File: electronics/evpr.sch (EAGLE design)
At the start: 93 parts, among them J1 10118193-0001LF, J2 B4P-VH(LF)(SN), Q1 AOD4184A, Q2 AOD4184A, T1 MMBT2222A, T2 MMBT2222A, T3 MMBT2222A, T5 MMBT2222A, U1 MC14044BDR2G, U2 BQ2057TTS, U3 ESP32-WROOM-32D, U5 AP2112K-3.3TRG1, U6 SN74AHCT125DR, U7 TPSM84824MOLR, U8 LTC4353CMSPBFMSOP-16_MS-M, X1 B3P-VH(LF)(SN), X2 B3P-VH(LF)(SN), X3 B3P-VH(LF)(SN)

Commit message: routing and board fixes
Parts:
- added U$13, U$15: LSM115J, mccloud:LSM115J
- C1: value 10sµF -> 10µF
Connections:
- new net AGND: R2.2, R31.2, R32.2, U7.AGND, U7.AGND_2, U7.AGND_3
- new net N$43: R7.2, R8.2, U$13.C, U$15.C, U1.!R1, U1.!R2, U1.!R3, U1.!S1, U1.!S2, U1.!S3, U1.E, U1.VDD
- net GND: no longer R2.2, R31.2, R32.2, U7.AGND, U7.AGND_2, U7.AGND_3
- net VBAT: now also U$15.A
- net VRAW: now also U$13.A; no longer R7.2, R8.2, U1.!R1, U1.!R2, U1.!R3, U1.!S1, U1.!S2, U1.!S3, U1.E, U1.VDD

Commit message: Whew. Lots of routing. Lots of minor circuit changes. Routing is 99% done, just finishing touches are remaining.
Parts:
- removed R11: 10k, rcl:R-US_R0805
- added C11, C21: 0.1uF, eagle-ltspice:CC0603
- U$13: value LSM115J -> SDM40E20LC; device mccloud:LSM115J -> mccloud:SDM40E20LC
- U$15: value LSM115J -> 1000µF; device mccloud:LSM115J -> mccloud:810RADCAP; COMPONENT (none) -> UWT0J102MNL1GS
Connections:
- net 5.0V: now also C21.2
- net GND: now also C11.1, C21.1, U$15.-; no longer R11.1
- net N$28: now also U$15.+
- net N$43: now also C11.2; no longer U$15.C
- net POWERSAVE: no longer R11.2
- net VBAT: now also U$13.A1; no longer U$15.A
- net VRAW: now also U$13.A2; no longer U$13.A
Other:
- moved on the sheet: F1, J2, JP1, U$2, U$7, X2, X3

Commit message: Routing complete. All DRC/ERC checks except for USB port silliness performed and resolved. Test points added.
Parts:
- added TP1, TP10, TP11, TP12, TP13, TP14, TP15, TP16, TP19, TP2, TP20, TP21, TP22, TP23, TP3, TP4, TP5, TP6, TP7, TP8, TP9: PTR1TP10R, testpad:PTR1TP10R
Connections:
- net 3.3V: now also TP12.TP
- net 5.0V: now also TP11.TP, U6.!1OE, U6.!2OE, U6.1A, U6.2A
- net AGND: now also TP7.TP
- net BOOTMODE: now also TP14.TP
- net GND: now also U6.!3OE, U6.!4OE
- net N$11: now also TP22.TP
- net N$14: now also TP10.TP
- net N$18: now also TP15.TP
- net N$19: now also TP16.TP
- net N$30: now also TP21.TP
- net N$35: now also TP8.TP
- net N$43: now also TP23.TP
- net N$51: now also TP9.TP
- net POWERSAVE: now also TP4.TP
- net RESET: now also TP13.TP
- net SHUTDOWN: now also TP19.TP
- net SHUTDOWN_CANCEL: now also TP20.TP
- net TACH_RAW: now also TP2.TP
- net USBD+: no longer J1.ID
- net VBAT: now also TP6.TP
- net VCONV: now also TP5.TP
- net VRAW: now also TP3.TP
- net VRAW_PF: now also TP1.TP
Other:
- moved on the sheet: C9, J1, R21, R23, R30

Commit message: Final  changes before prototype run
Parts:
- removed TP1: PTR1TP10R, testpad:PTR1TP10R
- removed U$6: 8A, mccloud:0437008.WR
- added SJ1: (no value), jumper:SJ
- added U$16: (no value), mccloud:VESD16A2-03G-G3-08
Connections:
- removed net VRAW_PF: TP1.TP, U$6.1, X1.2
- net GND: now also SJ1.1, U$16.AA
- net N$30: now also SJ1.2
- net SYS_POWER: now also Q1.D, Q2.D; no longer Q1.S, Q2.S
- net TACH_RAW: now also U$16.K1
- net VBAT: now also Q2.S; no longer Q2.D
- net VCONV: now also Q1.S; no longer Q1.D
- net VRAW: now also U$16.K2, X1.2; no longer U$6.2
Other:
- moved on the sheet: C6, C7, C8, LED1, Q1, Q2, R15, R20, R21, R22, R23, U8

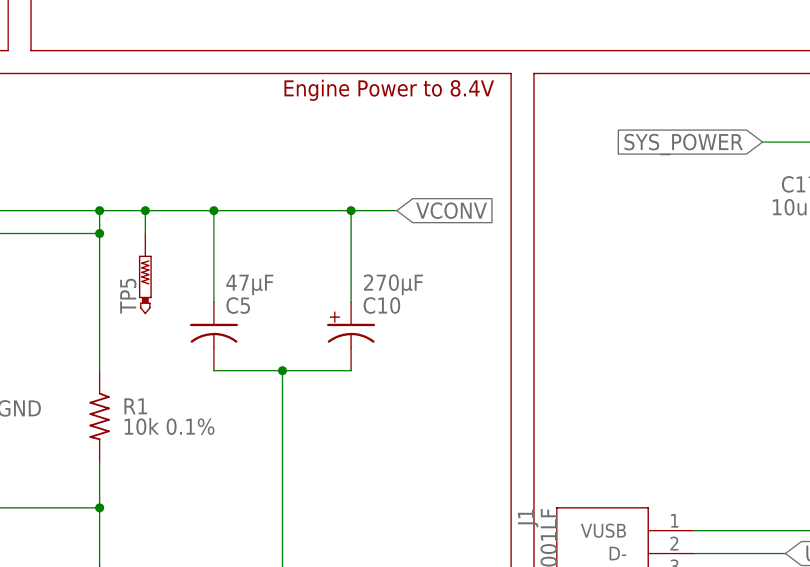
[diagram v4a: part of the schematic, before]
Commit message: Updated all part numbers, created BOM, created order recommendation
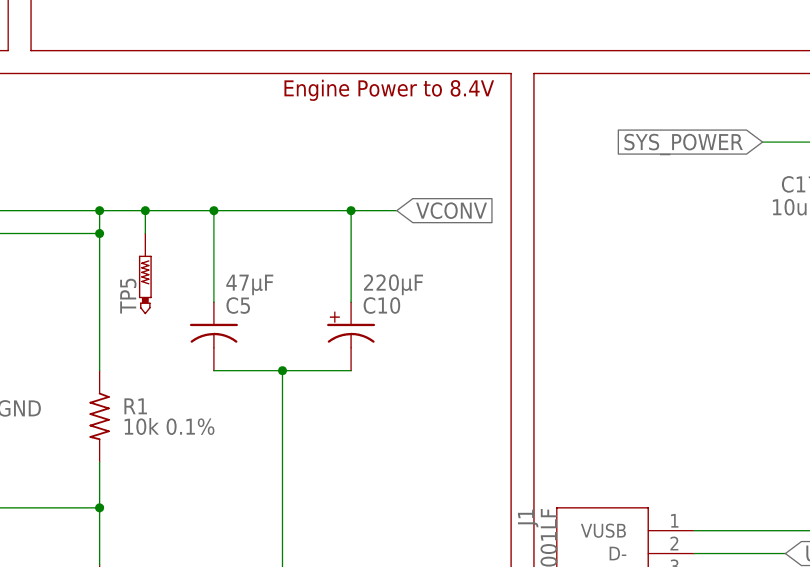
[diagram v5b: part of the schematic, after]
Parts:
- C1, C2: COMPONENT (none) -> C3225X7R1E106K250AC
- C10: value 270µF -> 220µF; COMPONENT (none) -> 875075355002
- C11, C12, C13, C21, C6: COMPONENT (none) -> 06033C104JAT2A
- C15, C20: COMPONENT (none) -> CL32A226MOJNNNE
- C16, C17, C18: COMPONENT (none) -> C1210C106M4PACTU
- C19: COMPONENT (none) -> C1210C105K5RAC7210
- C3, C4: COMPONENT (none) -> 25SVPF56M
- C7, C8: COMPONENT (none) -> CL10B562KB8NNNC
- C9: COMPONENT (none) -> CC0603CRNPO9BN4R7
- F1: COMPONENT Bel Fuse C1Q 1 -> C1Q 1
- J1: COMPONENT (none) -> 10118193-0001LF
- J2: COMPONENT (none) -> B4P-VH(LF)(SN)
- JP1: COMPONENT (none) -> 61300211021
- LED1: COMPONENT (none) -> LTST-C171GKT
- Q1, Q2: COMPONENT (none) -> AOD4184A
- R1: COMPONENT (none) -> PTN0805E1002BST1
- R10, R13, R14, R28, R9: COMPONENT (none) -> CR0805-JW-103ELF
- R12, R4: COMPONENT (none) -> RC0805JR-071KL
- R15: COMPONENT (none) -> CRCW0805499RFKEAHP
- R16, R17: COMPONENT (none) -> CRCW0805249RFKEAHP
- R18, R21, R23, R25, R27: COMPONENT (none) -> RNCP0805FTD22K1
- R19, R24, R26: COMPONENT (none) -> RC0805FR-0747K5L
- R2: COMPONENT (none) -> RC0402FR-07768RL
- R22, R29, R33, R34, R5, R6, R7, R8: COMPONENT (none) -> RC0805FR-07100KL
- R3: COMPONENT (none) -> CSR0603FKR250
- R30: COMPONENT (none) -> RC0805FR-071ML
- R31: COMPONENT (none) -> RC0201FR-0737K4L
- R32: COMPONENT (none) -> RC0805FR-0795K3L
- T1, T2, T3, T5: COMPONENT (none) -> MMBT2222A-7-F
- U$1: COMPONENT (none) -> PTS645SM43SMTR92 LFS
- U$10, U$8: COMPONENT (none) -> LSM115J
- U$11, U$4: COMPONENT (none) -> DMN5L06K-7
- U$12: COMPONENT (none) -> CP2102N-A02-GQFN24R
- U$14: COMPONENT (none) -> LBM2016T4R7J
- U$16: COMPONENT (none) -> VESD16A2-03G-G3-08
- U$2: COMPONENT (none) -> AP63205WU-7
- U$3: COMPONENT (none) -> STD2805
- U$5, U$9: COMPONENT (none) -> BSS84-7-F
- U1: COMPONENT (none) -> MC14044BDR2G
- U2: COMPONENT (none) -> BQ2057TTS
- U3: COMPONENT (none) -> ESP32-WROOM-32D
- U5: COMPONENT (none) -> AP2112K-3.3TRG1
- U6: COMPONENT (none) -> SN74AHCT125DR
- U7: COMPONENT (none) -> TPSM84824MOLR
- U8: COMPONENT (none) -> LTC4353CMS#PBF
- X1, X2, X3: COMPONENT (none) -> B3P-VH(LF)(SN)
- XA1, XA2: COMPONENT (none) -> B2P-VH(LF)(SN)

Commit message: Update serial interface chip to only receive power from USB plug, utilize internal regulator instead of board 3.3V regulator. Also update bypass caps to be to spec. Also added .gitignore for electronics folder.
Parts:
- added C22, C23: 0.1uF, eagle-ltspice:CC0603
- added C24: 4.7uF, eagle-ltspice:CC0603
- C16: value 10uF -> 4.7uF; device eagle-ltspice:CC1210 -> eagle-ltspice:CC0603; COMPONENT C1210C106M4PACTU -> CL10A475MQ8NNNC
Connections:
- removed net N$14: J1.VUSB, R16.2, R18.2, TP10.TP, U$10.A
- new net N$39: R12.2, U$12.VIO
- new net N$40: C16.2, C22.2, U$12.VDD
- new net VUSB: C23.2, C24.2, J1.VUSB, R16.2, R18.2, TP10.TP, U$10.A, U$12.VREGIN
- net 3.3V: no longer C16.1, R12.2, U$12.VDD, U$12.VIO, U$12.VREGIN
- net GND: now also C16.1, C22.1, C23.1, C24.1; no longer C16.2
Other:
- moved on the sheet: C16, C21, F1, J2, JP1, R10, R12, R13, R14, SV5, T3, T5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

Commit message: Completely redid sub 8V power path to support ESP32 deep-sleep as primary powersave mechagnism.
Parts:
- removed R29, R8: 100k, rcl:R-US_R0805
- removed SJ1: (no value), jumper:SJ
- removed T1, T2: MMBT2222A, transistor-neu-to92:MMBT2222ALT1-NPN-SOT23-BEC
- removed TP19, TP20, TP21, TP22, TP23: PTR1TP10R, testpad:PTR1TP10R
- removed U$14: 4.7µH, mccloud:LBM2016T4R7J
- removed U1: MC14044BDR2G, mccloud:MC14044BDR2G
- removed U5: AP2112K-3.3TRG1, mccloud:AP2112K-3.3TRG1
- added C25, C26: 0.1uF, eagle-ltspice:CC0603
- added TP1, TP17: PTR1TP10R, testpad:PTR1TP10R
- added U$17: (no value), mccloud:AP63205
- added U$19: 3.9µH, mccloud:SRR4818A-XXXX
- added U$20: 4.7µH, mccloud:SRR4818A-XXXX
- added U$6: SMD34LHE1, mccloud:SMD34LHE1
- C11: value 0.1uF -> 22uF; device eagle-ltspice:CC0603 -> eagle-ltspice:CC1210; COMPONENT 06033C104JAT2A -> CL32A226MOJNNNE
- C14: value 0.01uF -> 10uF; device eagle-ltspice:CC0603 -> eagle-ltspice:CC1210; COMPONENT (none) -> C1210C106M4PACTU
- C18: value 10uF -> 0.1uF; device eagle-ltspice:CC1210 -> eagle-ltspice:CC0603; COMPONENT C1210C106M4PACTU -> 06033C104JAT2A
- C19: value 1uF -> 22uF; COMPONENT C1210C105K5RAC7210 -> CL32A226MOJNNNE
- R7: value 100k -> 10k; COMPONENT RC0805FR-07100KL -> CR0805-JW-103ELF
- U$10, U$8: value LSM115J -> SMD34LHE1; device mccloud:LSM115J -> mccloud:SMD34LHE1; COMPONENT LSM115J -> SMD34LHE1-TP
- U$13: value SDM40E20LC -> SMD34LHE1; device mccloud:SDM40E20LC -> mccloud:SMD34LHE1; COMPONENT (none) -> SMD34LHE1-TP
- U$7: value R3119N050A-TR-FE -> SMD34LHE1; device mccloud:R3119N050A-TR-FE -> mccloud:SMD34LHE1; COMPONENT (none) -> SMD34LHE1-TP
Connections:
- removed net 3.3V: C18.1, C19.1, R28.1, R9.1, TP12.TP, U3.3V3, U5.VOUT
- removed net N$11: R8.1, T1.C, TP22.TP, U$7.D_OUT, U1.!S0
- removed net N$12: R7.1, T2.C, U1.!R0
- removed net N$30: SJ1.2, TP21.TP, U1.Q0, U8.!EN1, U8.!EN2
- removed net N$43: C11.2, R7.2, R8.2, TP23.TP, U$13.C, U1.!R1, U1.!R2, U1.!R3, U1.!S1, U1.!S2, U1.!S3, U1.E, U1.VDD
- removed net N$9: C14.1, U$7.CD
- new net BUILTIN_LED: R16.2
- new net ESP_POWER: C11.1, C19.1, R28.1, R7.1, R9.1, TP12.TP, U$17.FB, U$19.2, U3.3V3
- new net LED_BUILTIN: U3.IO12
- new net N$14: C18.1, U$17.BST
- new net N$41: C14.1, C25.2, TP17.TP, U$10.C, U$13.C, U$17.EN, U$17.VIN, U$8.C
- new net SYS_POW_EN: R7.2, TP1.TP, U8.!EN1, U8.!EN2
- net 5.0V: now also U$6.C, U$7.C; no longer R29.1, U$10.C, U$8.C, U5.VIN
- net CSTAT: no longer U3.IO12
- net GND: now also C11.2, C25.1, C26.1, U$17.GND; no longer C11.1, C18.2, SJ1.1, T1.E, T2.E, U$7.GND, U1.VSS, U5.GND
- net N$26: now also C18.2, U$17.SW, U$19.1; no longer R29.2, U5.EN
- net N$47: no longer U3.IO5
- net N$50: now also U$20.1; no longer U$14.1
- net N$51: now also U$20.2, U$7.A; no longer U$14.2, U$8.A
- net SHUTDOWN: no longer T2.B, TP19.TP
- net SHUTDOWN_CANCEL: no longer T1.B, TP20.TP
- net SYS_POWER: now also C26.2
- net VBAT: now also U$13.A; no longer U$13.A1
- net VCONV: now also U$8.A
- net VRAW: no longer U$13.A2, U$7.V_DD
- net VUSB: now also U$6.A; no longer R16.2
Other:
- note added: "5V Power Management"
- note added: "ESP32 / Deep Sleep Power"
- note added: "ESP32 Reset"
- note added: "ESP32 USB Serial / Programming Interface"
- note added: "NOTE: LED_BUILTIN will blink during flashing. This is why the LED circuit is included here, rather than in the ESP32 block."
- note added: "SYS_POWER Management"
- note removed: "Power Merge & Control"
- note removed: "USB & Low Voltage Power"
- note removed: "USB Serial / Programming Interface"
- moved on the sheet: C1, C10, C11, C12, C13, C14, C15, C16, C17, C18, C19, C2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

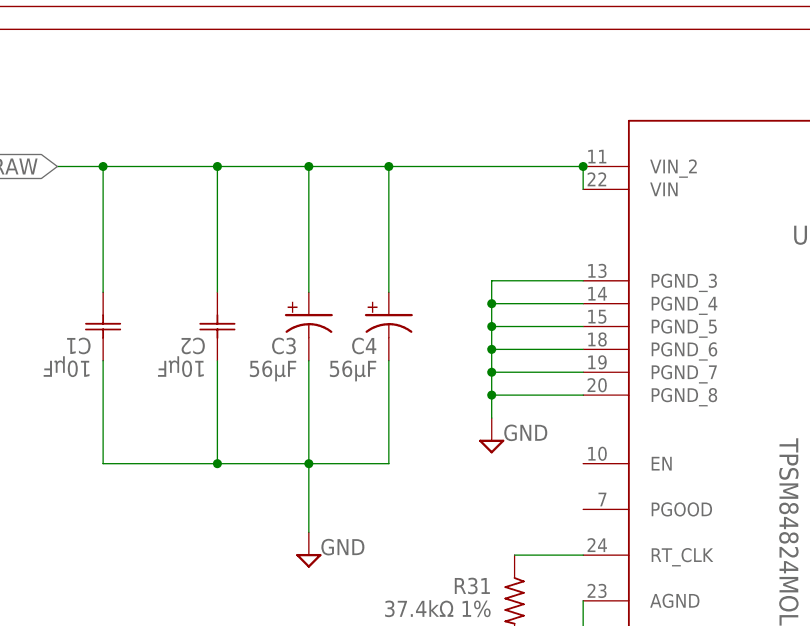
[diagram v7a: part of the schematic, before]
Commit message: Switched C3 and C4 to alternative capacitor
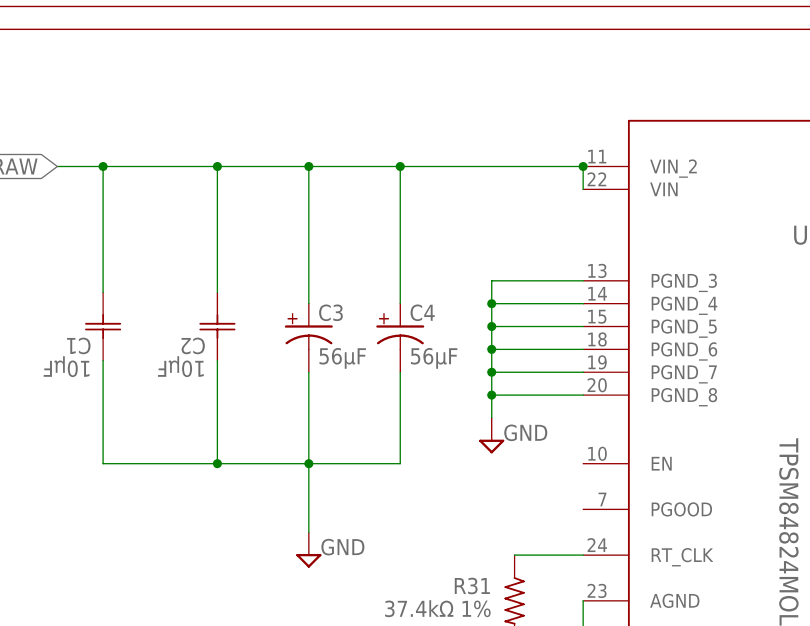
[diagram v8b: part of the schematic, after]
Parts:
- C3, C4: device mccloud:25SVPF56M -> mccloud:6.3MMCAP; COMPONENT 25SVPF56M -> APXG250ARA560MF61G
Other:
- moved on the sheet: C3, C4
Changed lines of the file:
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@@
 <attribute name="COMPONENT" value="C3225X7R1E106K250AC"/>
-</part>
-<part name="C3" library="mccloud" deviceset="25SVPF56M" device="" value="56µF">
-<attribute name="COMPONENT" value="25SVPF56M"/>
-</part>
-<part name="C4" library="mccloud" deviceset="25SVPF56M" device="" value="56µF">
-<attribute name="COMPONENT" value="25SVPF56M"/>
 </part>
 <part name="SUPPLY32" library="supply2" library_urn="urn:adsk.eagle:library:372" deviceset="GND" device=""/>
@@
 </part>
 <part name="TP17" library="testpad" library_urn="urn:adsk.eagle:library:385" deviceset="PTR1" device="TP10R" package3d_urn="urn:adsk.eagle:package:27959/1" value="PTR1TP10R"/>
+<part name="C3" library="mccloud" deviceset="6.3MMCAP" device="" value="56µF">
+<attribute name="COMPONENT" value="APXG250ARA560MF61G"/>
+</part>
+<part name="C4" library="mccloud" deviceset="6.3MMCAP" device="" value="56µF">
+<attribute name="COMPONENT" value="APXG250ARA560MF61G"/>
+</part>
 </parts>
 <sheets>
@@
 <attribute name="COMPONENT" x="-180.34" y="-20.32" size="1.778" layer="96" rot="R90" display="off"/>
 </instance>
-<instance part="C3" gate="G$1" x="-170.18" y="-19.05" smashed="yes">
-<attribute name="NAME" x="-171.45" y="-21.59" size="1.78071875" layer="95" rot="R180"/>
-<attribute name="VALUE" x="-171.45" y="-24.13" size="1.77813125" layer="96" rot="R180"/>
-<attribute name="COMPONENT" x="-170.18" y="-19.05" size="1.778" layer="96" display="off"/>
-</instance>
-<instance part="C4" gate="G$1" x="-161.29" y="-19.05" smashed="yes">
-<attribute name="NAME" x="-162.56" y="-21.59" size="1.78071875" layer="95" rot="R180"/>
-<attribute name="VALUE" x="-162.56" y="-24.13" size="1.77813125" layer="96" rot="R180"/>
-<attribute name="COMPONENT" x="-161.29" y="-19.05" size="1.778" layer="96" display="off"/>
-</instance>
 <instance part="SUPPLY32" gate="GND" x="-170.18" y="-45.72" smashed="yes">
 <attribute name="VALUE" x="-168.91" y="-45.72" size="1.778" layer="96"/>
@@
 <attribute name="NAME" x="110.744" y="19.05" size="1.778" layer="95" rot="R90"/>
 <attribute name="TP_SIGNAL_NAME" x="113.03" y="22.86" size="1.778" layer="97"/>
+</instance>
+<instance part="C3" gate="G$1" x="-170.18" y="-20.32" smashed="yes">
+<attribute name="NAME" x="-169.162440625" y="-19.684028125" size="1.78071875" layer="95"/>
+<attribute name="VALUE" x="-169.16393125" y="-24.511309375" size="1.77813125" layer="96"/>
+<attribute name="COMPONENT" x="-170.18" y="-20.32" size="1.778" layer="96" display="off"/>
+</instance>
+<instance part="C4" gate="G$1" x="-160.02" y="-20.32" smashed="yes">
+<attribute name="NAME" x="-159.002440625" y="-19.684028125" size="1.78071875" layer="95"/>
+<attribute name="VALUE" x="-159.00393125" y="-24.511309375" size="1.77813125" layer="96"/>
+<attribute name="COMPONENT" x="-160.02" y="-20.32" size="1.778" layer="96" display="off"/>
 </instance>
 </instances>
@@
 <pinref part="C2" gate="G$1" pin="1"/>
 <wire x1="-180.34" y1="-35.56" x2="-180.34" y2="-24.13" width="0.1524" layer="91"/>
-<pinref part="C3" gate="G$1" pin="-"/>
-<wire x1="-170.18" y1="-24.13" x2="-170.18" y2="-35.56" width="0.1524" layer="91"/>
 <wire x1="-170.18" y1="-35.56" x2="-180.34" y2="-35.56" width="0.1524" layer="91"/>
 <junction x="-180.34" y="-35.56"/>
-<pinref part="C4" gate="G$1" pin="-"/>
-<wire x1="-161.29" y1="-24.13" x2="-161.29" y2="-35.56" width="0.1524" layer="91"/>
-<wire x1="-161.29" y1="-35.56" x2="-170.18" y2="-35.56" width="0.1524" layer="91"/>
 <junction x="-170.18" y="-35.56"/>
+<wire x1="-160.02" y1="-35.56" x2="-170.18" y2="-35.56" width="0.1524" layer="91"/>
 <wire x1="-170.18" y1="-35.56" x2="-170.18" y2="-43.18" width="0.1524" layer="91"/>
 <pinref part="SUPPLY32" gate="GND" pin="GND"/>
+<pinref part="C3" gate="G$1" pin="-"/>
+<wire x1="-170.18" y1="-25.4" x2="-170.18" y2="-35.56" width="0.1524" layer="91"/>
+<pinref part="C4" gate="G$1" pin="-"/>
+<wire x1="-160.02" y1="-35.56" x2="-160.02" y2="-25.4" width="0.1524" layer="91"/>
 </segment>
 <segment>
@@
 <pinref part="U7" gate="A" pin="VIN_2"/>
 <wire x1="-139.7" y1="-5.08" x2="-139.7" y2="-2.54" width="0.1524" layer="91"/>
-<wire x1="-139.7" y1="-2.54" x2="-161.29" y2="-2.54" width="0.1524" layer="91"/>
+<wire x1="-139.7" y1="-2.54" x2="-160.02" y2="-2.54" width="0.1524" layer="91"/>
 <junction x="-139.7" y="-2.54"/>
 <pinref part="C1" gate="G$1" pin="2"/>
-<wire x1="-161.29" y1="-2.54" x2="-170.18" y2="-2.54" width="0.1524" layer="91"/>
+<wire x1="-160.02" y1="-2.54" x2="-170.18" y2="-2.54" width="0.1524" layer="91"/>
 <wire x1="-170.18" y1="-2.54" x2="-180.34" y2="-2.54" width="0.1524" layer="91"/>
 <wire x1="-180.34" y1="-2.54" x2="-193.04" y2="-2.54" width="0.1524" layer="91"/>
@@
 <wire x1="-180.34" y1="-16.51" x2="-180.34" y2="-2.54" width="0.1524" layer="91"/>
 <junction x="-180.34" y="-2.54"/>
-<wire x1="-170.18" y1="-16.51" x2="-170.18" y2="-2.54" width="0.1524" layer="91"/>
 <junction x="-170.18" y="-2.54"/>
-<wire x1="-161.29" y1="-16.51" x2="-161.29" y2="-2.54" width="0.1524" layer="91"/>
-<junction x="-161.29" y="-2.54"/>
-<pinref part="C3" gate="G$1" pin="+"/>
-<pinref part="C4" gate="G$1" pin="+"/>
+<wire x1="-170.18" y1="-17.78" x2="-170.18" y2="-2.54" width="0.1524" layer="91"/>
 <wire x1="-193.04" y1="-2.54" x2="-198.12" y2="-2.54" width="0.1524" layer="91"/>
 <junction x="-193.04" y="-2.54"/>
 <label x="-198.12" y="-2.54" size="1.778" layer="95" rot="R180" xref="yes"/>
-</segment>
-<segment>
+<pinref part="C4" gate="G$1" pin="+"/>
+<wire x1="-160.02" y1="-17.78" x2="-160.02" y2="-2.54" width="0.1524" layer="91"/>
+<junction x="-160.02" y="-2.54"/>
+<pinref part="C3" gate="G$1" pin="+"/>
+</segment>
+<segment>
